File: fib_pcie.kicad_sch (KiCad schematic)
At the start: 59 parts, among them J901 Bus_M.2_2199230-6, J902 Bus_M.2_1-2199230-6, Y1 ECS-327ATQ2520MV-32.786K

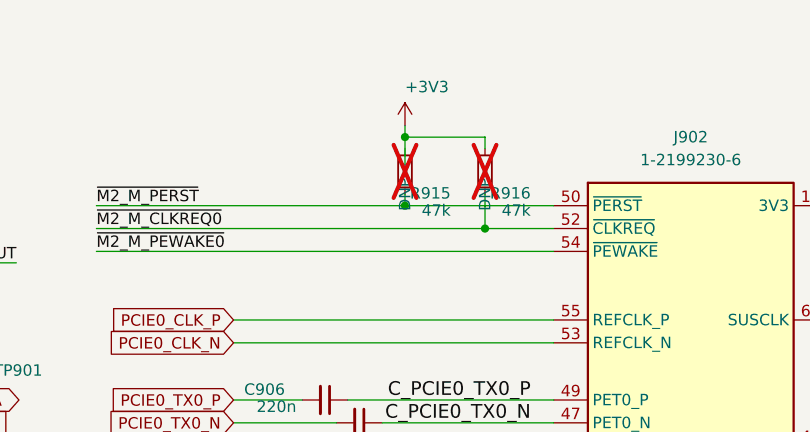
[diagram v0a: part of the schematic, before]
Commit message: added port expander and level shifters, routed peripherals fixed most drc errors, assigned gpios etc.
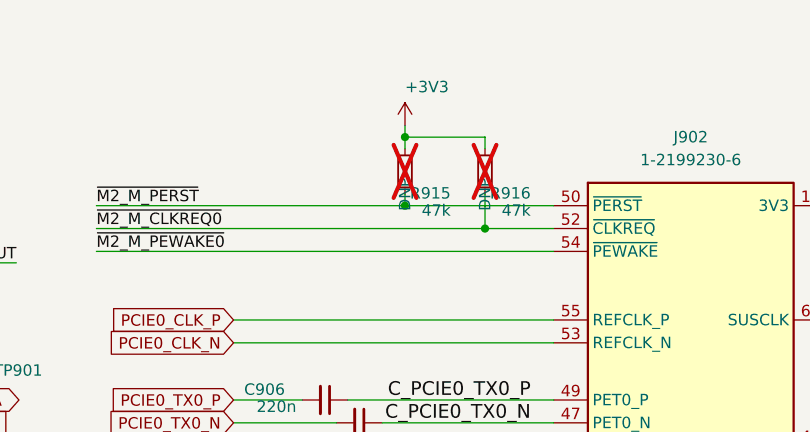
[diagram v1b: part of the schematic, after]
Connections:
- net +3V3: now also R915.1
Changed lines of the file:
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@@
+	(wire
+		(pts
+			(xy 184.15 29.21) (xy 184.15 30.48)
+		)
+		(stroke
+			(width 0)
+			(type default)
+		)
+	)
 	(wire
 		(pts
@@
 	(wire
 		(pts
+			(xy 184.15 30.48) (xy 184.15 31.75)
+		)
+		(stroke
+			(width 0)
+			(type default)
+		)
+	)
+	(wire
+		(pts
 			(xy 165.1 62.23) (xy 176.53 62.23)
 		)
@@
 	(wire
 		(pts
-			(xy 184.15 30.48) (xy 184.15 34.29)
-		)
-		(stroke
-			(width 0)
-			(type default)
-		)
-	)
-	(wire
-		(pts
 			(xy 231.14 138.43) (xy 220.98 138.43)
 		)
@@
 		)
 		(stroke
-			(width 0)
-			(type default)
-		)
-	)
-	(wire
-		(pts
-			(xy 184.15 30.48) (xy 184.15 29.21)
-		)
-		(stroke
